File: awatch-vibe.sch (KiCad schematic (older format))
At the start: 8 parts

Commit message: annotate all
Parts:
- gave numbers to parts that had none: 8
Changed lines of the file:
@@
 $EndDescr
 $Comp
-L awatch-parts:DRV2604 U?
+L awatch-parts:DRV2604 U901
 U 1 1 5C7D39BF
 P 5150 3850
-F 0 "U?" H 5300 3150 50  0000 C CNN
+F 0 "U901" H 5300 3150 50  0000 C CNN
 F 1 "DRV2604" H 5900 3150 50  0000 C CNN
 F 2 "" H 5150 3850 50  0001 C CNN
@@
 	5650 3800 5650 3550
 $Comp
-L power:+3V8 #PWR?
+L power:+3V8 #PWR0200
 U 1 1 5C7D41CC
 P 5650 3550
-F 0 "#PWR?" H 5650 3400 50  0001 C CNN
+F 0 "#PWR0200" H 5650 3400 50  0001 C CNN
 F 1 "+3V8" H 5665 3723 50  0000 C CNN
 F 2 "" H 5650 3550 50  0001 C CNN
@@
 $EndComp
 $Comp
-L Device:C_Small C?
+L Device:C_Small C903
 U 1 1 5C7D4208
 P 6300 3700
-F 0 "C?" H 6392 3746 50  0000 L CNN
+F 0 "C903" H 6392 3746 50  0000 L CNN
 F 1 "1µF" H 6392 3655 50  0000 L CNN
 F 2 "" H 6300 3700 50  0001 C CNN
@@
 	5750 3500 6300 3500
 $Comp
-L power:GND #PWR?
+L power:GND #PWR0201
 U 1 1 5C7D42C4
 P 5650 4750
-F 0 "#PWR?" H 5650 4500 50  0001 C CNN
+F 0 "#PWR0201" H 5650 4500 50  0001 C CNN
 F 1 "GND" H 5655 4577 50  0000 C CNN
 F 2 "" H 5650 4750 50  0001 C CNN
@@
 	5650 4750 5650 4600
 $Comp
-L power:GND #PWR?
+L power:GND #PWR0202
 U 1 1 5C7D436F
 P 6300 3850
-F 0 "#PWR?" H 6300 3600 50  0001 C CNN
+F 0 "#PWR0202" H 6300 3600 50  0001 C CNN
 F 1 "GND" H 6305 3677 50  0000 C CNN
 F 2 "" H 6300 3850 50  0001 C CNN
@@
 	6300 3800 6300 3850
 $Comp
-L Device:R_Small_US R?
+L Device:R_Small_US R901
 U 1 1 5C7D4436
 P 4400 4250
-F 0 "R?" V 4195 4250 50  0000 C CNN
+F 0 "R901" V 4195 4250 50  0000 C CNN
 F 1 "0" V 4286 4250 50  0000 C CNN
 F 2 "" H 4400 4250 50  0001 C CNN
@@
 $EndComp
 $Comp
-L Device:R_Small_US R?
+L Device:R_Small_US R902
 U 1 1 5C7D446D
 P 4400 4350
-F 0 "R?" V 4195 4350 50  0000 C CNN
+F 0 "R902" V 4195 4350 50  0000 C CNN
 F 1 "0" V 4286 4350 50  0000 C CNN
 F 2 "" H 4400 4350 50  0001 C CNN
@@
 	4150 4350 4300 4350
 $Comp
-L Device:R_Small_US R?
+L Device:R_Small_US R904
 U 1 1 5C7D45B8
 P 4900 4550
-F 0 "R?" H 4832 4504 50  0000 R CNN
+F 0 "R904" H 4832 4504 50  0000 R CNN
 F 1 "0" H 4832 4595 50  0000 R CNN
 F 2 "" H 4900 4550 50  0001 C CNN
@@
 	4900 4150 4900 4450
 $Comp
-L power:GND #PWR?
+L power:GND #PWR0203
 U 1 1 5C7D467F
 P 4900 4750
-F 0 "#PWR?" H 4900 4500 50  0001 C CNN
+F 0 "#PWR0203" H 4900 4500 50  0001 C CNN
 F 1 "GND" H 4905 4577 50  0000 C CNN
 F 2 "" H 4900 4750 50  0001 C CNN
@@
 	4900 4750 4900 4700
 $Comp
-L Device:R_Small_US R?
+L Device:R_Small_US R903
 U 1 1 5C7D4778
 P 4650 4550
-F 0 "R?" H 4582 4504 50  0000 R CNN
+F 0 "R903" H 4582 4504 50  0000 R CNN
 F 1 "0" H 4582 4595 50  0000 R CNN
 F 2 "" H 4650 4550 50  0001 C CNN
@@
 	6150 4250 6550 4250
 $Comp
-L Device:C_Small C?
+L Device:C_Small C901
 U 1 1 5C7D4FD4
 P 4200 3500
-F 0 "C?" H 4292 3546 50  0000 L CNN
+F 0 "C901" H 4292 3546 50  0000 L CNN
 F 1 "1µF" H 4292 3455 50  0000 L CNN
 F 2 "" H 4200 3500 50  0001 C CNN
@@
 $EndComp
 $Comp
-L Device:C_Small C?
+L Device:C_Small C902
 U 1 1 5C7D4FFF
 P 4600 3500
-F 0 "C?" H 4692 3546 50  0000 L CNN
+F 0 "C902" H 4692 3546 50  0000 L CNN
 F 1 "0.1µF" H 4692 3455 50  0000 L CNN
 F 2 "" H 4600 3500 50  0001 C CNN
@@
 $EndComp
 $Comp
-L power:+3V8 #PWR?
+L power:+3V8 #PWR0204
 U 1 1 5C7D503D
 P 4200 3250
-F 0 "#PWR?" H 4200 3100 50  0001 C CNN
+F 0 "#PWR0204" H 4200 3100 50  0001 C CNN
 F 1 "+3V8" H 4215 3423 50  0000 C CNN
 F 2 "" H 4200 3250 50  0001 C CNN
@@
 	4200 3350 4200 3400
 $Comp
-L power:GND #PWR?
+L power:GND #PWR0205
 U 1 1 5C7D5481
 P 4200 3750
-F 0 "#PWR?" H 4200 3500 50  0001 C CNN
+F 0 "#PWR0205" H 4200 3500 50  0001 C CNN
 F 1 "GND" H 4205 3577 50  0000 C CNN
 F 2 "" H 4200 3750 50  0001 C CNN
@@
 	4200 3650 4200 3750
 $Comp
-L power:+3V8 #PWR?
+L power:+3V8 #PWR0206
 U 1 1 5C7D639D
 P 6950 2800
-F 0 "#PWR?" H 6950 2650 50  0001 C CNN
+F 0 "#PWR0206" H 6950 2650 50  0001 C CNN
 F 1 "+3V8" H 6965 2973 50  0000 C CNN
 F 2 "" H 6950 2800 50  0001 C CNN
@@
 $EndComp
 $Comp
-L power:GND #PWR?
+L power:GND #PWR0207
 U 1 1 5C7D63B8
 P 6950 3100
-F 0 "#PWR?" H 6950 2850 50  0001 C CNN
+F 0 "#PWR0207" H 6950 2850 50  0001 C CNN
 F 1 "GND" H 6955 2927 50  0000 C CNN
 F 2 "" H 6950 3100 50  0001 C CNN

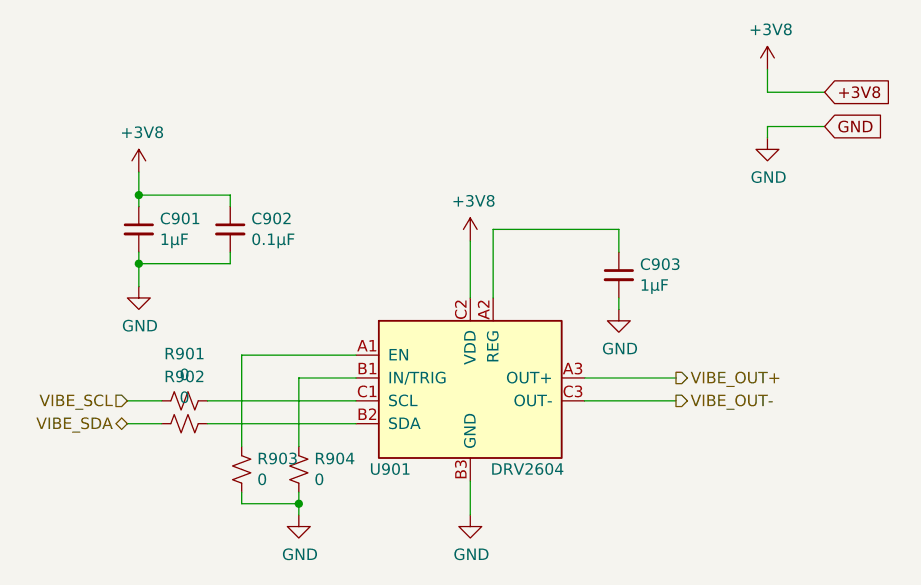
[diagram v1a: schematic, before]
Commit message: add power measurement cuts
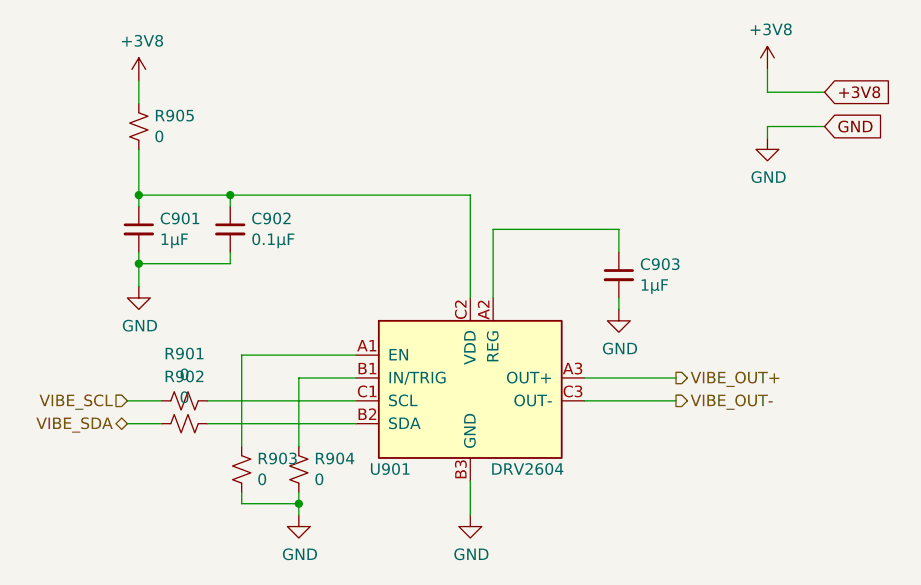
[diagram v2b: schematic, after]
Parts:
- added R905: 0, symbol Device:R_Small_US
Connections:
- net +3V8: now also R905.2; no longer C901.1, C902.1, U901.C2 (VDD)
- new net: C901.1, C902.1, R905.1, U901.C2 (VDD)
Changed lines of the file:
@@
-	1    0    0    -1
-$EndComp
-Wire Wire Line
-	5650 3800 5650 3550
-$Comp
-L power:+3V8 #PWR0200
-U 1 1 5C7D41CC
-P 5650 3550
-F 0 "#PWR0200" H 5650 3400 50  0001 C CNN
-F 1 "+3V8" H 5665 3723 50  0000 C CNN
-F 2 "" H 5650 3550 50  0001 C CNN
-F 3 "" H 5650 3550 50  0001 C CNN
-	1    5650 3550
 	1    0    0    -1
 $EndComp
@@
 L power:+3V8 #PWR0204
 U 1 1 5C7D503D
-P 4200 3250
-F 0 "#PWR0204" H 4200 3100 50  0001 C CNN
-F 1 "+3V8" H 4215 3423 50  0000 C CNN
-F 2 "" H 4200 3250 50  0001 C CNN
-F 3 "" H 4200 3250 50  0001 C CNN
-	1    4200 3250
-	1    0    0    -1
-$EndComp
-Wire Wire Line
-	4200 3250 4200 3350
+P 4200 2850
+F 0 "#PWR0204" H 4200 2700 50  0001 C CNN
+F 1 "+3V8" H 4215 3023 50  0000 C CNN
+F 2 "" H 4200 2850 50  0001 C CNN
+F 3 "" H 4200 2850 50  0001 C CNN
+	1    4200 2850
+	1    0    0    -1
+$EndComp
 Wire Wire Line
 	4200 3350 4600 3350
@@
 Wire Wire Line
 	6950 2900 7200 2900
+$Comp
+L Device:R_Small_US R905
+U 1 1 5C7E118E
+P 4200 3050
+F 0 "R905" H 4132 3004 50  0000 R CNN
+F 1 "0" H 4132 3095 50  0000 R CNN
+F 2 "" H 4200 3050 50  0001 C CNN
+F 3 "~" H 4200 3050 50  0001 C CNN
+	1    4200 3050
+	-1   0    0    1
+$EndComp
+Wire Wire Line
+	4200 2850 4200 2950
+Wire Wire Line
+	4200 3150 4200 3350
+Wire Wire Line
+	4600 3350 5650 3350
+Wire Wire Line
+	5650 3350 5650 3800
+Connection ~ 4600 3350
 $EndSCHEMATC

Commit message: Add footprints.
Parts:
- C901, C902, C903: footprint (none) -> Capacitor_SMD:C_0603_1608Metric
- R901, R902, R903, R904, R905: footprint (none) -> Resistor_SMD:R_0603_1608Metric
- U901: footprint (none) -> awatch2-footprints:Texas_DSBGA-9_1.47x1.47mm_Layout3x3_P0.5mm_NSMD
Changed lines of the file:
@@
 EESchema Schematic File Version 4
+LIBS:awatch2-cache
 EELAYER 26 0
 EELAYER END
@@
 F 0 "U901" H 5300 3150 50  0000 C CNN
 F 1 "DRV2604" H 5900 3150 50  0000 C CNN
-F 2 "" H 5150 3850 50  0001 C CNN
+F 2 "awatch2-footprints:Texas_DSBGA-9_1.47x1.47mm_Layout3x3_P0.5mm_NSMD" H 5150 3850 50  0001 C CNN
 F 3 "" H 5150 3850 50  0001 C CNN
 	1    5150 3850
@@
 F 0 "C903" H 6392 3746 50  0000 L CNN
 F 1 "1µF" H 6392 3655 50  0000 L CNN
-F 2 "" H 6300 3700 50  0001 C CNN
+F 2 "Capacitor_SMD:C_0603_1608Metric" H 6300 3700 50  0001 C CNN
 F 3 "~" H 6300 3700 50  0001 C CNN
 	1    6300 3700
@@
 F 0 "R901" V 4195 4250 50  0000 C CNN
 F 1 "0" V 4286 4250 50  0000 C CNN
-F 2 "" H 4400 4250 50  0001 C CNN
+F 2 "Resistor_SMD:R_0603_1608Metric" H 4400 4250 50  0001 C CNN
 F 3 "~" H 4400 4250 50  0001 C CNN
 	1    4400 4250
@@
 F 0 "R902" V 4195 4350 50  0000 C CNN
 F 1 "0" V 4286 4350 50  0000 C CNN
-F 2 "" H 4400 4350 50  0001 C CNN
+F 2 "Resistor_SMD:R_0603_1608Metric" H 4400 4350 50  0001 C CNN
 F 3 "~" H 4400 4350 50  0001 C CNN
 	1    4400 4350
@@
 F 0 "R904" H 4832 4504 50  0000 R CNN
 F 1 "0" H 4832 4595 50  0000 R CNN
-F 2 "" H 4900 4550 50  0001 C CNN
+F 2 "Resistor_SMD:R_0603_1608Metric" H 4900 4550 50  0001 C CNN
 F 3 "~" H 4900 4550 50  0001 C CNN
 	1    4900 4550
@@
 F 0 "R903" H 4582 4504 50  0000 R CNN
 F 1 "0" H 4582 4595 50  0000 R CNN
-F 2 "" H 4650 4550 50  0001 C CNN
+F 2 "Resistor_SMD:R_0603_1608Metric" H 4650 4550 50  0001 C CNN
 F 3 "~" H 4650 4550 50  0001 C CNN
 	1    4650 4550
@@
 F 0 "C901" H 4292 3546 50  0000 L CNN
 F 1 "1µF" H 4292 3455 50  0000 L CNN
-F 2 "" H 4200 3500 50  0001 C CNN
+F 2 "Capacitor_SMD:C_0603_1608Metric" H 4200 3500 50  0001 C CNN
 F 3 "~" H 4200 3500 50  0001 C CNN
 	1    4200 3500
@@
 F 0 "C902" H 4692 3546 50  0000 L CNN
 F 1 "0.1µF" H 4692 3455 50  0000 L CNN
-F 2 "" H 4600 3500 50  0001 C CNN
+F 2 "Capacitor_SMD:C_0603_1608Metric" H 4600 3500 50  0001 C CNN
 F 3 "~" H 4600 3500 50  0001 C CNN
 	1    4600 3500
@@
 F 0 "R905" H 4132 3004 50  0000 R CNN
 F 1 "0" H 4132 3095 50  0000 R CNN
-F 2 "" H 4200 3050 50  0001 C CNN
+F 2 "Resistor_SMD:R_0603_1608Metric" H 4200 3050 50  0001 C CNN
 F 3 "~" H 4200 3050 50  0001 C CNN
 	1    4200 3050

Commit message: vibe, mic, display P&R
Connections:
- net VIBE_EN: now reaches R903.2, U901.A1 (EN)
- net VIBE_REG: now reaches C903.1, U901.A2 (REG)
- net VIBE_IN: now reaches R904.2, U901.B1 (IN/TRIG)
- net VIBE_SDA_IN: now reaches R902.1, U901.B2 (SDA)
- net VIBE_SCL_IN: now reaches R901.1, U901.C1 (SCL)
- net VIBE_VDD: now reaches C901.1, C902.1, R905.1, U901.C2 (VDD)
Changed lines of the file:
@@
 	5650 3350 5650 3800
 Connection ~ 4600 3350
+Text Label 5850 3500 0    50   ~ 0
+VIBE_REG
+Text Label 4950 3350 0    50   ~ 0
+VIBE_VDD
+Text Label 4750 4250 0    50   ~ 0
+VIBE_SCL_IN
+Text Label 4750 4350 0    50   ~ 0
+VIBE_SDA_IN
+Text Label 4750 4050 0    50   ~ 0
+VIBE_EN
+Text Label 4900 4150 0    50   ~ 0
+VIBE_IN
 $EndSCHEMATC

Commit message: approx. final layout
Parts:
- C901, C903: value 1µF -> 1.0µF X7R; DigiKey PN (none) -> 1276-1946-1-ND
- C902: value 0.1µF -> 0.1µF X7R; DigiKey PN (none) -> 1276-1061-1-ND
- U901: DigiKey PN (none) -> 296-45407-1-ND
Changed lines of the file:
@@
 $Descr A4 11693 8268
 encoding utf-8
-Sheet 9 9
+Sheet 9 10
 Title "AWatch2"
 Date ""
@@
 F 2 "awatch2-footprints:Texas_DSBGA-9_1.47x1.47mm_Layout3x3_P0.5mm_NSMD" H 5150 3850 50  0001 C CNN
 F 3 "" H 5150 3850 50  0001 C CNN
+F 4 "296-45407-1-ND" H 0   0   50  0001 C CNN "DigiKey PN"
 	1    5150 3850
 	1    0    0    -1
@@
 P 6300 3700
 F 0 "C903" H 6392 3746 50  0000 L CNN
-F 1 "1µF" H 6392 3655 50  0000 L CNN
+F 1 "1.0µF X7R" H 6392 3655 50  0000 L CNN
 F 2 "Capacitor_SMD:C_0603_1608Metric" H 6300 3700 50  0001 C CNN
 F 3 "~" H 6300 3700 50  0001 C CNN
+F 4 "1276-1946-1-ND" H 0   0   50  0001 C CNN "DigiKey PN"
 	1    6300 3700
 	1    0    0    -1
@@
 P 4200 3500
 F 0 "C901" H 4292 3546 50  0000 L CNN
-F 1 "1µF" H 4292 3455 50  0000 L CNN
+F 1 "1.0µF X7R" H 4292 3455 50  0000 L CNN
 F 2 "Capacitor_SMD:C_0603_1608Metric" H 4200 3500 50  0001 C CNN
 F 3 "~" H 4200 3500 50  0001 C CNN
+F 4 "1276-1946-1-ND" H 0   0   50  0001 C CNN "DigiKey PN"
 	1    4200 3500
 	1    0    0    -1
@@
 P 4600 3500
 F 0 "C902" H 4692 3546 50  0000 L CNN
-F 1 "0.1µF" H 4692 3455 50  0000 L CNN
+F 1 "0.1µF X7R" H 4692 3455 50  0000 L CNN
 F 2 "Capacitor_SMD:C_0603_1608Metric" H 4600 3500 50  0001 C CNN
 F 3 "~" H 4600 3500 50  0001 C CNN
+F 4 "1276-1061-1-ND" H 0   0   50  0001 C CNN "DigiKey PN"
 	1    4600 3500
 	1    0    0    -1

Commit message: BOM fully populated
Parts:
- R901, R902, R903, R904, R905: DigiKey PN (none) -> MCT0603-0.0-ZZCT-ND
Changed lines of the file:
@@
 F 2 "Resistor_SMD:R_0603_1608Metric" H 4400 4250 50  0001 C CNN
 F 3 "~" H 4400 4250 50  0001 C CNN
+F 4 "MCT0603-0.0-ZZCT-ND" H 0   0   50  0001 C CNN "DigiKey PN"
 	1    4400 4250
 	0    1    1    0
@@
 F 2 "Resistor_SMD:R_0603_1608Metric" H 4400 4350 50  0001 C CNN
 F 3 "~" H 4400 4350 50  0001 C CNN
+F 4 "MCT0603-0.0-ZZCT-ND" H 0   0   50  0001 C CNN "DigiKey PN"
 	1    4400 4350
 	0    1    1    0
@@
 F 2 "Resistor_SMD:R_0603_1608Metric" H 4900 4550 50  0001 C CNN
 F 3 "~" H 4900 4550 50  0001 C CNN
+F 4 "MCT0603-0.0-ZZCT-ND" H 0   0   50  0001 C CNN "DigiKey PN"
 	1    4900 4550
 	-1   0    0    1
@@
 F 2 "Resistor_SMD:R_0603_1608Metric" H 4650 4550 50  0001 C CNN
 F 3 "~" H 4650 4550 50  0001 C CNN
+F 4 "MCT0603-0.0-ZZCT-ND" H 0   0   50  0001 C CNN "DigiKey PN"
 	1    4650 4550
 	-1   0    0    1
@@
 F 2 "Resistor_SMD:R_0603_1608Metric" H 4200 3050 50  0001 C CNN
 F 3 "~" H 4200 3050 50  0001 C CNN
+F 4 "MCT0603-0.0-ZZCT-ND" H 0   0   50  0001 C CNN "DigiKey PN"
 	1    4200 3050
 	-1   0    0    1
